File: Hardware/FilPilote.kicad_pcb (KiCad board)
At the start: 2 copper layers, 50 x 50 mm, 38 parts, among them IC1 MOC3041M, IC2 MOC3041M, IC3 MOC3041M, IC4 MOC3041M, IC5 MOC3041M, IC6 MOC3041M, P1 CONN_01X03, P2 CONN_01X03, P3 CONN_01X07

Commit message: Remove useless earth connection
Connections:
- P1 pad 1: Terre -> (no net)
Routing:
- net GND: track 77.9 -> 119.6 mm, vias 0 -> 2
- net Net-(IC5-Pad1): track 36.8 -> 29.1 mm
- net Phase: track 125.8 -> 132.9 mm
- removed copper zone on B.Cu, net Terre
- removed copper zone on F.Cu, net Terre
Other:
- board text removed: "Terre"

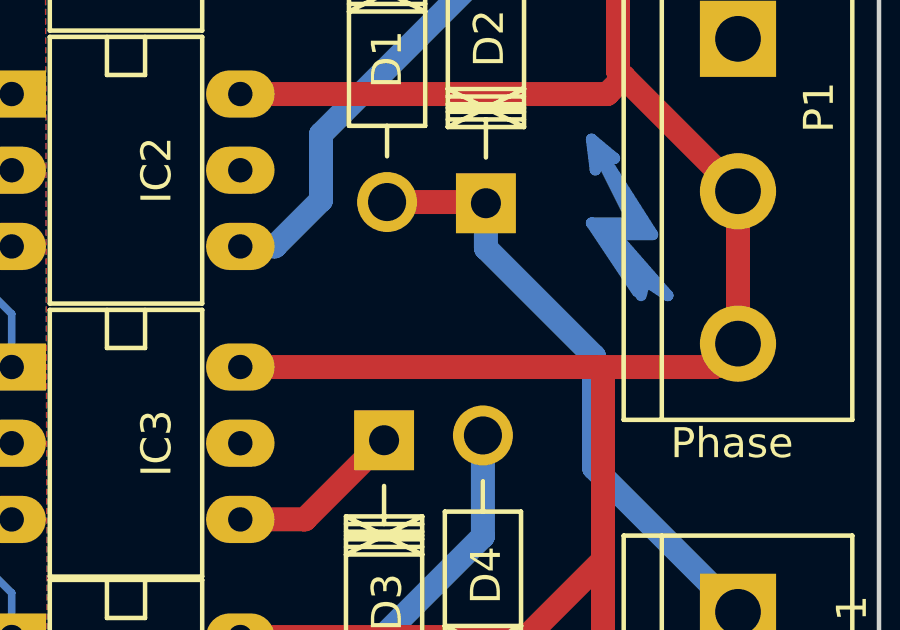
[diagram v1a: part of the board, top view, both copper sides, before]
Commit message: Label "Danger!"
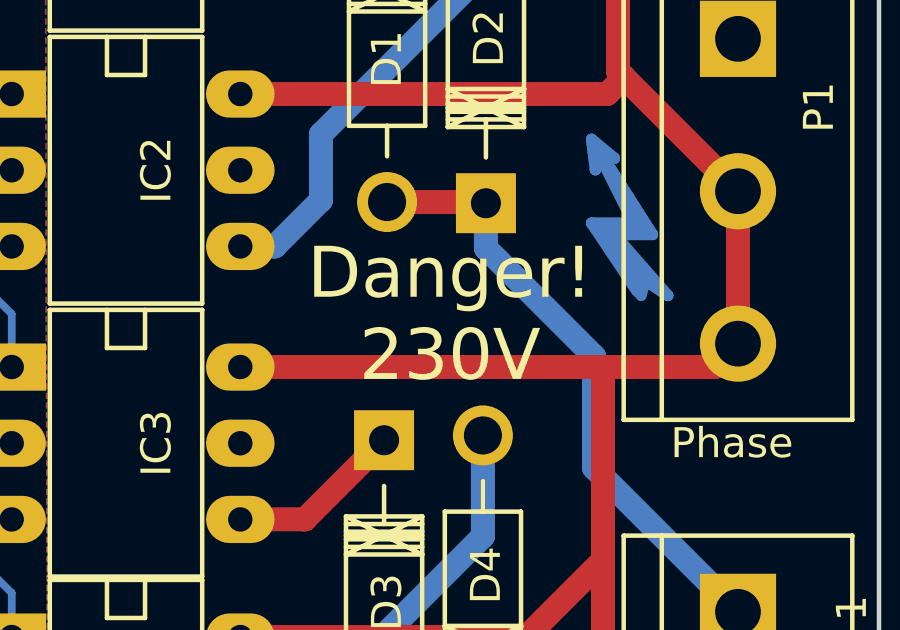
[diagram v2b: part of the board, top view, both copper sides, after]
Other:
- board text added: "Danger! 230V"

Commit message: Move to kicad 4.0.0 RC1
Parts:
- D1, D2, D3, D4, D5, D6: footprint Diodes_ThroughHole:Diode_DO-41_SOD81_Horizontal_RM10 -> Discret:D4
- moved D6 6.84 mm to (64.8, 66.0), turned to 90 degrees
- moved D2 5.70 mm to (64.8, 33.0)
- moved D5 5.59 mm to (61.0, 66.0), turned to 270 degrees
- moved D3 5.47 mm to (61.0, 52.1)
- moved D4 4.57 mm to (64.8, 52.1)
- moved D1 4.52 mm to (61.0, 33.0)
- moved D10 2.54 mm to (28.8, 50.7), turned to 0 degrees
- moved D11 2.54 mm to (28.8, 59.7), turned to 0 degrees
- moved D12 2.54 mm to (28.8, 68.7), turned to 0 degrees
- moved D7 2.54 mm to (28.8, 46.2), turned to 0 degrees
- moved D8 2.54 mm to (28.8, 55.2), turned to 0 degrees
- moved D9 2.54 mm to (28.8, 64.2), turned to 0 degrees
- moved REF** 1.10 mm to (69.3, 38.7)
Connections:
- D10 pad 1: Net-(D10-Pad1) -> GND
- D10 pad 2: GND -> Net-(D10-Pad2)
- D11 pad 1: Net-(D11-Pad1) -> GND
- D11 pad 2: GND -> Net-(D11-Pad2)
- D12 pad 1: Net-(D12-Pad1) -> GND
- D12 pad 2: GND -> Net-(D12-Pad2)
- D7 pad 1: Net-(D7-Pad1) -> GND
- D7 pad 2: GND -> Net-(D7-Pad2)
- D8 pad 1: Net-(D8-Pad1) -> GND
- D8 pad 2: GND -> Net-(D8-Pad2)
- D9 pad 1: Net-(D9-Pad1) -> GND
- D9 pad 2: GND -> Net-(D9-Pad2)
- P1 pad 1: (no net) -> Net-(P1-Pad1)
- R10 pad 2: Net-(D7-Pad1) -> Net-(D7-Pad2)
- R11 pad 2: Net-(D8-Pad1) -> Net-(D8-Pad2)
- R12 pad 2: Net-(D9-Pad1) -> Net-(D9-Pad2)
- R7 pad 2: Net-(D10-Pad1) -> Net-(D10-Pad2)
- R8 pad 2: Net-(D11-Pad1) -> Net-(D11-Pad2)
- R9 pad 2: Net-(D12-Pad1) -> Net-(D12-Pad2)
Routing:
- net FP1: track 20.4 -> 31.5 mm
- net Net-(D12-Pad2): track 0.00 -> 7.99 mm
- net Net-(D12-Pad1): track 7.99 -> 0.00 mm
- net FP2: track 12.2 -> 18.6 mm
- net Net-(D9-Pad2): track 0.00 -> 6.38 mm
- net Net-(D9-Pad1): track 6.38 -> 0.00 mm
- net Net-(D4-Pad2): track 15.8 -> 9.49 mm
- net Net-(D11-Pad2): track 0.00 -> 6.28 mm
- net Net-(D11-Pad1): track 6.28 -> 0.00 mm
- net Net-(D2-Pad2): track 15.7 -> 9.50 mm
- net Net-(D3-Pad1): track 5.89 -> 11.4 mm
- net Net-(D8-Pad2): track 0.00 -> 4.48 mm
- net Net-(D8-Pad1): track 4.48 -> 0.00 mm
- net Net-(D6-Pad2): track 18.0 -> 22.4 mm
- net Net-(D7-Pad2): track 0.00 -> 4.36 mm
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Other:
- board text added: "G"

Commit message: Add fabrication files
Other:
- board text added: "Interface pour Fil Pilote - v2.0"
- board text removed: "Interface pour Fil Pilote"
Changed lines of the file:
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@@
     (links 55)
     (no_connects 0)
-    (area 27.324999 23.824999 77.475001 73.975001)
+    (area 24.837667 18.825 88.058334 76.33026)
     (thickness 1.6)
-    (drawings 24)
+    (drawings 29)
     (tracks 204)
     (zones 0)
@@
   )
   (page A4)
+  (title_block
+    (title "Interface pour fil pilote")
+    (date 2015-10-10)
+    (rev v2.0)
+  )
   (layers
     (0 F.Cu signal)
@@
   )
   (setup
-    (last_trace_width 0.8)
+    (last_trace_width 0.254)
     (user_trace_width 0.8)
     (trace_clearance 0.254)
@@
     (visible_elements FFFFFF7F)
     (pcbplotparams
-      (layerselection 0x00030_80000001)
-      (usegerberextensions false)
-      (excludeedgelayer true)
+      (layerselection 0x010f0_80000001)
+      (usegerberextensions true)
+      (excludeedgelayer false)
       (linewidth 0.800000)
       (plotframeref false)
@@
       (outputformat 1)
       (mirror false)
-      (drillshape 1)
+      (drillshape 0)
       (scaleselection 1)
-      (outputdirectory ""))
+      (outputdirectory fabrication/))
   )
   (net 0 "")
@@
     )
   )
+  (gr_line (start 37.5 63.9) (end 37.5 73.8) (angle 90) (layer F.SilkS) (width 0.2))
+  (gr_line (start 42.8 63.9) (end 37.5 63.9) (angle 90) (layer F.SilkS) (width 0.2))
+  (gr_line (start 48 69.1) (end 42.8 63.9) (angle 90) (layer F.SilkS) (width 0.2))
+  (gr_line (start 50.2 69.1) (end 48 69.1) (angle 90) (layer F.SilkS) (width 0.2))
+  (gr_line (start 50.2 24) (end 50.2 69.1) (angle 90) (layer F.SilkS) (width 0.2))
   (gr_line (start 37.5 63.9) (end 37.5 73.8) (angle 90) (layer B.SilkS) (width 0.2))
   (gr_line (start 42.8 63.9) (end 37.5 63.9) (angle 90) (layer B.SilkS) (width 0.2))
@@
     (effects (font (size 1 1) (thickness 0.25)) (justify mirror))
   )
-  (gr_text "Interface pour Fil Pilote" (at 51.5 34.3 90) (layer B.SilkS)
+  (gr_text "Interface pour Fil Pilote - v2.0" (at 51.5 37.3 90) (layer B.SilkS)
     (effects (font (size 1 1) (thickness 0.25)) (justify mirror))
   )
@@
   (gr_line (start 77.4 73.9) (end 27.4 73.9) (angle 90) (layer Edge.Cuts) (width 0.15))
   (gr_line (start 77.4 23.9) (end 77.4 73.9) (angle 90) (layer Edge.Cuts) (width 0.15))
-  (dimension 50 (width 0.25) (layer F.SilkS)
-    (gr_text "50,000 mm" (at 83.6 48.9 270) (layer F.SilkS)
+  (dimension 50 (width 0.25) (layer Dwgs.User)
+    (gr_text "50,000 mm" (at 83.6 48.9 270) (layer Dwgs.User)
       (effects (font (size 1 1) (thickness 0.25)))
     )
@@
     (arrow2b (pts (xy 82.6 23.9) (xy 83.186421 25.026504)))
   )
-  (dimension 50 (width 0.25) (layer F.SilkS)
-    (gr_text "50,000 mm" (at 52.5 19.9) (layer F.SilkS)
+  (dimension 50 (width 0.25) (layer Dwgs.User)
+    (gr_text "50,000 mm" (at 52.5 19.9) (layer Dwgs.User)
       (effects (font (size 1 1) (thickness 0.25)))
     )
